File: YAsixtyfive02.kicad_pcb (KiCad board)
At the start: 2 copper layers, 99.7 x 99.7 mm, 59 parts, among them J1 ~{NMI}, J2 Aux 5VDC, J3 Power 5V, J4 Expansion Bus, J7 GND, J8 FTDI Serial2USB, SW1 RESET, SW2 SW_Push_DPDT, U1 WD65C02, U10 74LS138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

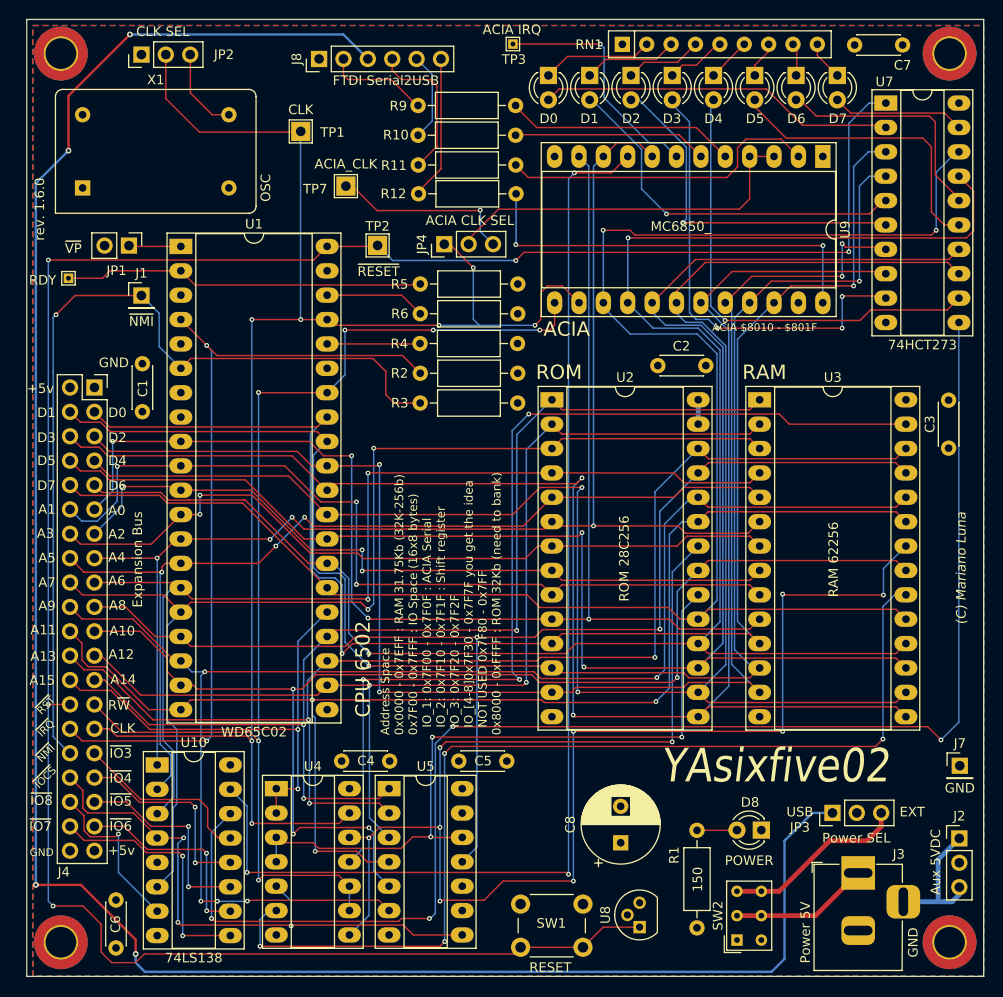
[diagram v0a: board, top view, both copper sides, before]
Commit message: rev 1.6.1 ready. minor routing updates and acia CS fixed.
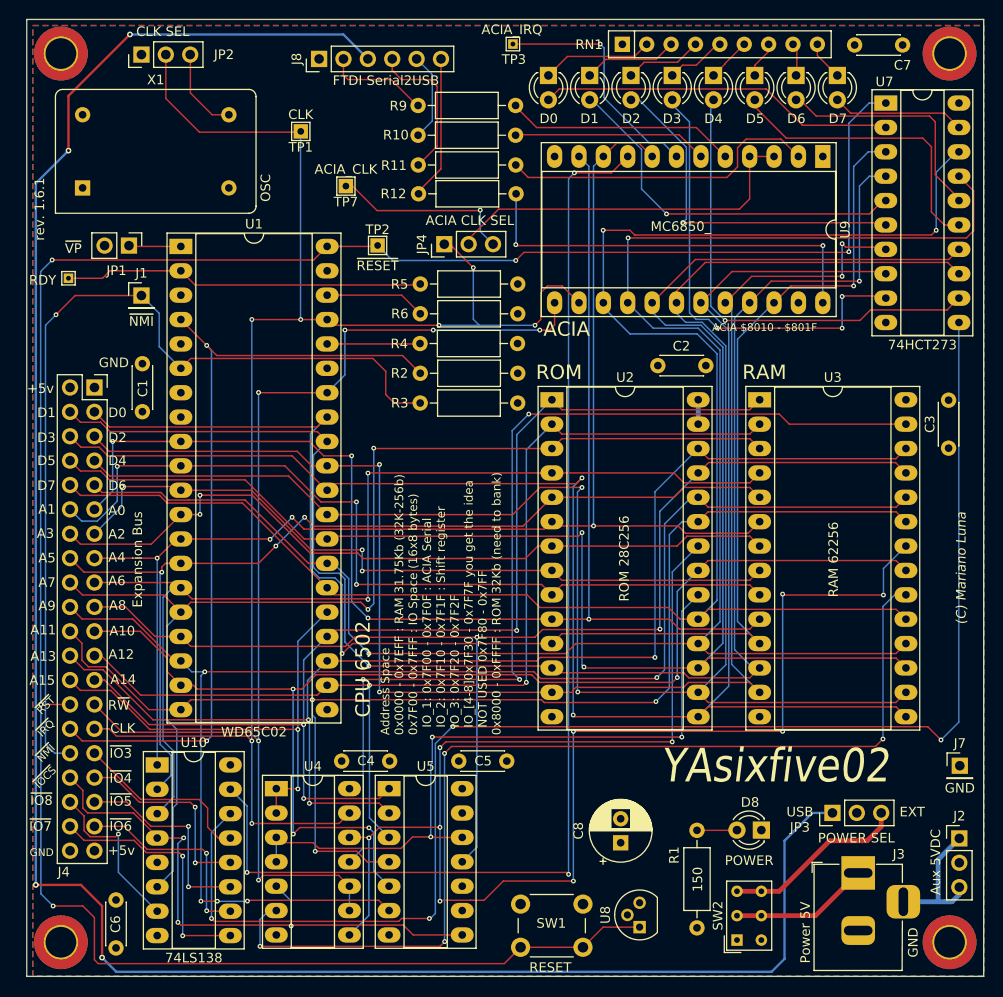
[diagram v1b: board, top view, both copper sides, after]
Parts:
- C8: footprint Capacitor_THT:CP_Radial_D8.0mm_P3.80mm -> Capacitor_THT:CP_Radial_D6.3mm_P2.50mm
- JP3: value Power SEL -> POWER SEL
- TP1, TP2, TP7: footprint TestPoint:TestPoint_THTPad_2.0x2.0mm_Drill1.0mm -> TestPoint:TestPoint_THTPad_1.5x1.5mm_Drill0.7mm
- TP3: value ACIA IRQ -> ACIA_IRQ
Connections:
- U10 pad 5: +5V -> GND
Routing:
- net ~{RESET}: track 239.7 -> 241.9 mm
- net USB_5V: track 220.7 -> 222.5 mm
- net ~{NMI}: track 94.3 -> 95.8 mm
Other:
- board text added: "rev. 1.6.1"
- board text removed: "rev. 1.6.0"
